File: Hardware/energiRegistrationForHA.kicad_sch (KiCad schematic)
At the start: 43 parts, among them J1 Screw_Terminal_01x04, J2 Screw_Terminal_01x04, J3 Screw_Terminal_01x04, Q1 S8050_NPN, Q2 S8050_NPN, Q3 S8050_NPN, Q4 S8050_NPN, U1 74HC14, U2 74HC14

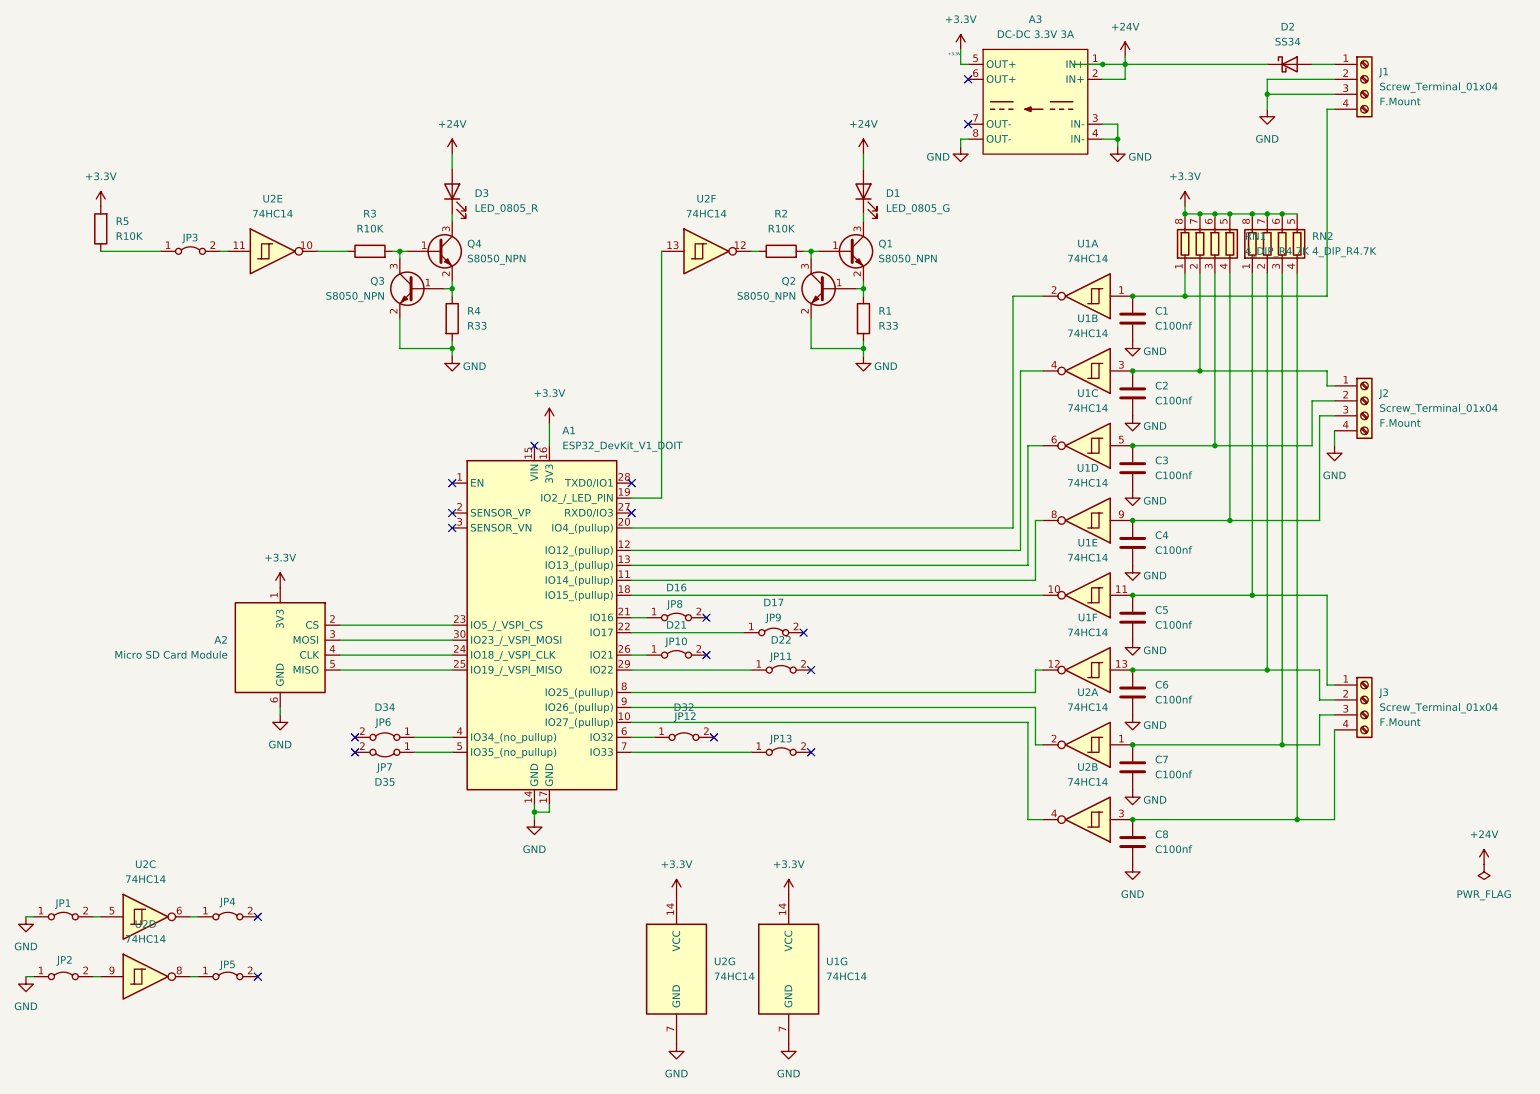
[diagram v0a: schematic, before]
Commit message: HW HEX Schmittrigger entered
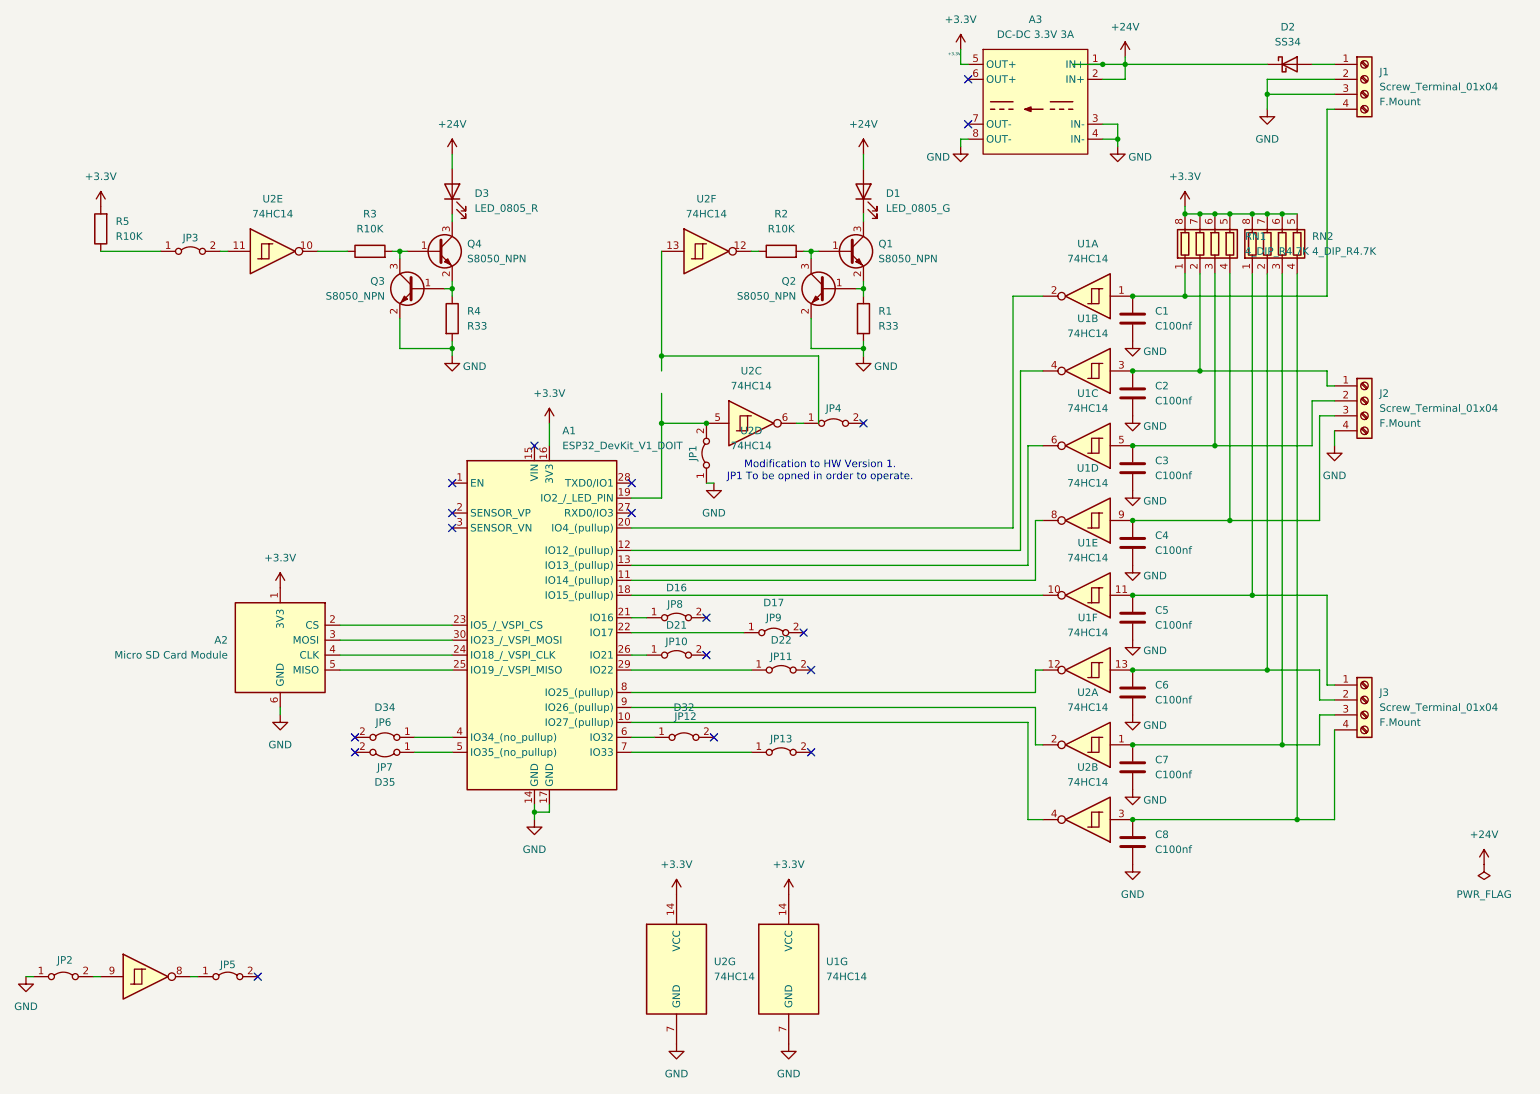
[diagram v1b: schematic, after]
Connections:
- net at A1.19 (IO2_/_LED_PIN): now also JP1.2 (B), U2.5; no longer U2.13
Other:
- note added: "Modification to HW Version 1. JP1 To be opned in order to operate."
- moved on the sheet: JP1, JP4, U2C
